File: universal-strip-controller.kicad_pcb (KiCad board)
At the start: 2 copper layers, 200 x 125 mm, 240 parts, among them J1 Conn_01x03_Pin, J10 DB301V-3.5-3P-GN, J11 DB301V-3.5-3P-GN, J12 DB301V-3.5-3P-GN, J13 DB301V-3.5-3P-GN, J14 DB301V-3.5-3P-GN, J15 DB301V-3.5-3P-GN, J16 DB301V-3.5-3P-GN, J17 DB301V-3.5-3P-GN, J18 DB301V-3.5-3P-GN, J19 DB301V-3.5-3P-GN, J2 Conn_01x02_Pin, J20 DB301V-3.5-3P-GN, J21 DB301V-3.5-3P-GN, J22 DB301V-3.5-3P-GN, J23 DB301V-3.5-3P-GN, J24 DB301V-3.5-3P-GN, J25 DB301V-3.5-3P-GN, J26 DB301V-3.5-3P-GN, J27 DB301V-3.5-3P-GN, J28 DB301V-3.5-3P-GN, J29 DB301V-3.5-3P-GN, J3 DBT50G-9.5-2P, J30 DB301V-3.5-3P-GN, J31 DB301V-3.5-3P-GN, J32 DB301V-3.5-3P-GN, J33 DB301V-3.5-3P-GN, J34 DB301V-3.5-3P-GN, J35 DB301V-3.5-3P-GN, J36 DB301V-3.5-3P-GN, J37 DB301V-3.5-3P-GN, J38 2.54-1*4, J39 DB301V-3.5-3P-GN, J4 DBT50G-9.5-2P, J5 DBT50G-9.5-2P, J6 DBT50G-9.5-2P, J7 DB301V-3.5-3P-GN, J8 DB301V-3.5-3P-GN, J9 DB301V-3.5-3P-GN, SW1 434133025816, SW2 434133025816, U1 RP2350B, U10 SN74LVC8T245PWR, U11 SN74LVC8T245PWR, U2 RPI RM2, U3 W25Q128JVSIQ, U4 SN74LVC1T45DBV, U5 TPS63070RNMR, U7 SN74LVC8T245PWR, U8 SN74LVC8T245PWR, U9 DS3231SN, X1 12MHz

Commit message: Working on layout
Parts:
- added C133: 100n, RPI_COMPILED:generic_capc1005x50, F.Cu at (209.5, 80.5)
- added C134: 100n, RPI_COMPILED:generic_capc1005x50, F.Cu at (209.5, 97.3)
- moved D12 371.3 mm to (214.3, 70.0), turned to 180 degrees
- moved C122 370.0 mm to (209.5, 72.0), turned to -90 degrees
- moved D16 362.8 mm to (214.3, 78.8), turned to 180 degrees
- moved C129 360.6 mm to (209.5, 88.5), turned to -90 degrees
- moved J23 360.1 mm to (226.5, 146.5), turned to 180 degrees
- moved D11 360.1 mm to (204.0, 70.0), turned to 180 degrees
- moved C121 359.4 mm to (199.0, 72.0), turned to -90 degrees
- moved C125 354.7 mm to (199.0, 80.5), turned to -90 degrees
- moved D20 354.6 mm to (214.3, 87.0), turned to 180 degrees
- moved C128 354.0 mm to (199.0, 88.5), turned to -90 degrees
- moved D15 351.7 mm to (204.0, 78.5), turned to 180 degrees
- moved C132 349.5 mm to (199.0, 97.5), turned to -90 degrees
- moved C120 349.4 mm to (189.0, 72.0), turned to -90 degrees
- moved D9 348.9 mm to (193.7, 70.0), turned to 180 degrees
- moved D24 346.5 mm to (214.3, 95.5), turned to 180 degrees
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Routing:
- net Net-(D11-DIN): track 0.00 -> 7.56 mm
- net Net-(D3-DOUT): track 0.00 -> 7.56 mm
- net Net-(D3-DIN): track 0.00 -> 5.36 mm
- net Net-(U4-B): track 0.00 -> 2.54 mm
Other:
- copper layers 2 -> 4

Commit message: Working on layout
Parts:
- moved F24 153.9 mm to (82.6, 150.8)
- moved J23 153.0 mm to (73.5, 148.6)
- moved J31 149.4 mm to (64.6, 133.2)
- moved F31 143.6 mm to (236.1, 150.8)
- moved J30 143.6 mm to (226.1, 148.6)
- moved F32 143.0 mm to (73.5, 137.9)
- moved J39 137.5 mm to (209.5, 133.2)
- moved F39 135.2 mm to (218.2, 139.2)
- moved F25 112.8 mm to (103.2, 150.8)
- moved J24 112.8 mm to (93.8, 148.6)
- moved F33 112.2 mm to (92.3, 137.9)
- moved J32 112.2 mm to (83.3, 133.2)
- moved J29 98.3 mm to (200.8, 148.6)
- moved F30 98.3 mm to (211.3, 150.8)
- moved F38 95.1 mm to (199.1, 137.9)
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
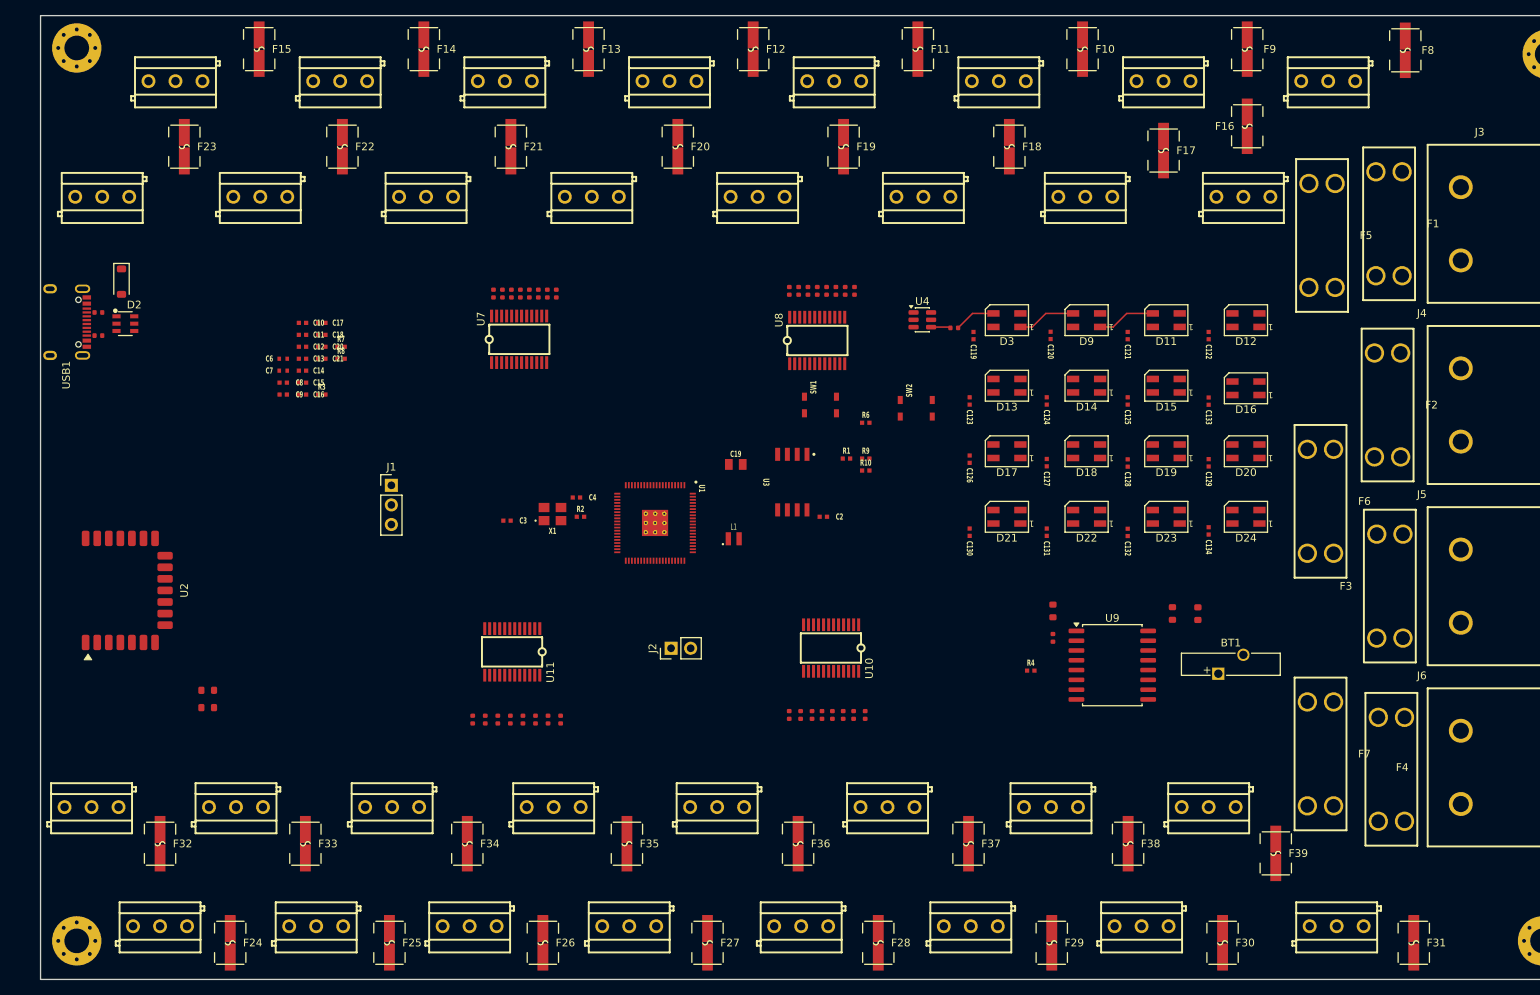
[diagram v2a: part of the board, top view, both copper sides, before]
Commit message: I think the output terminals are well-arranged now. Discovered pixel-blits layout all on my own.
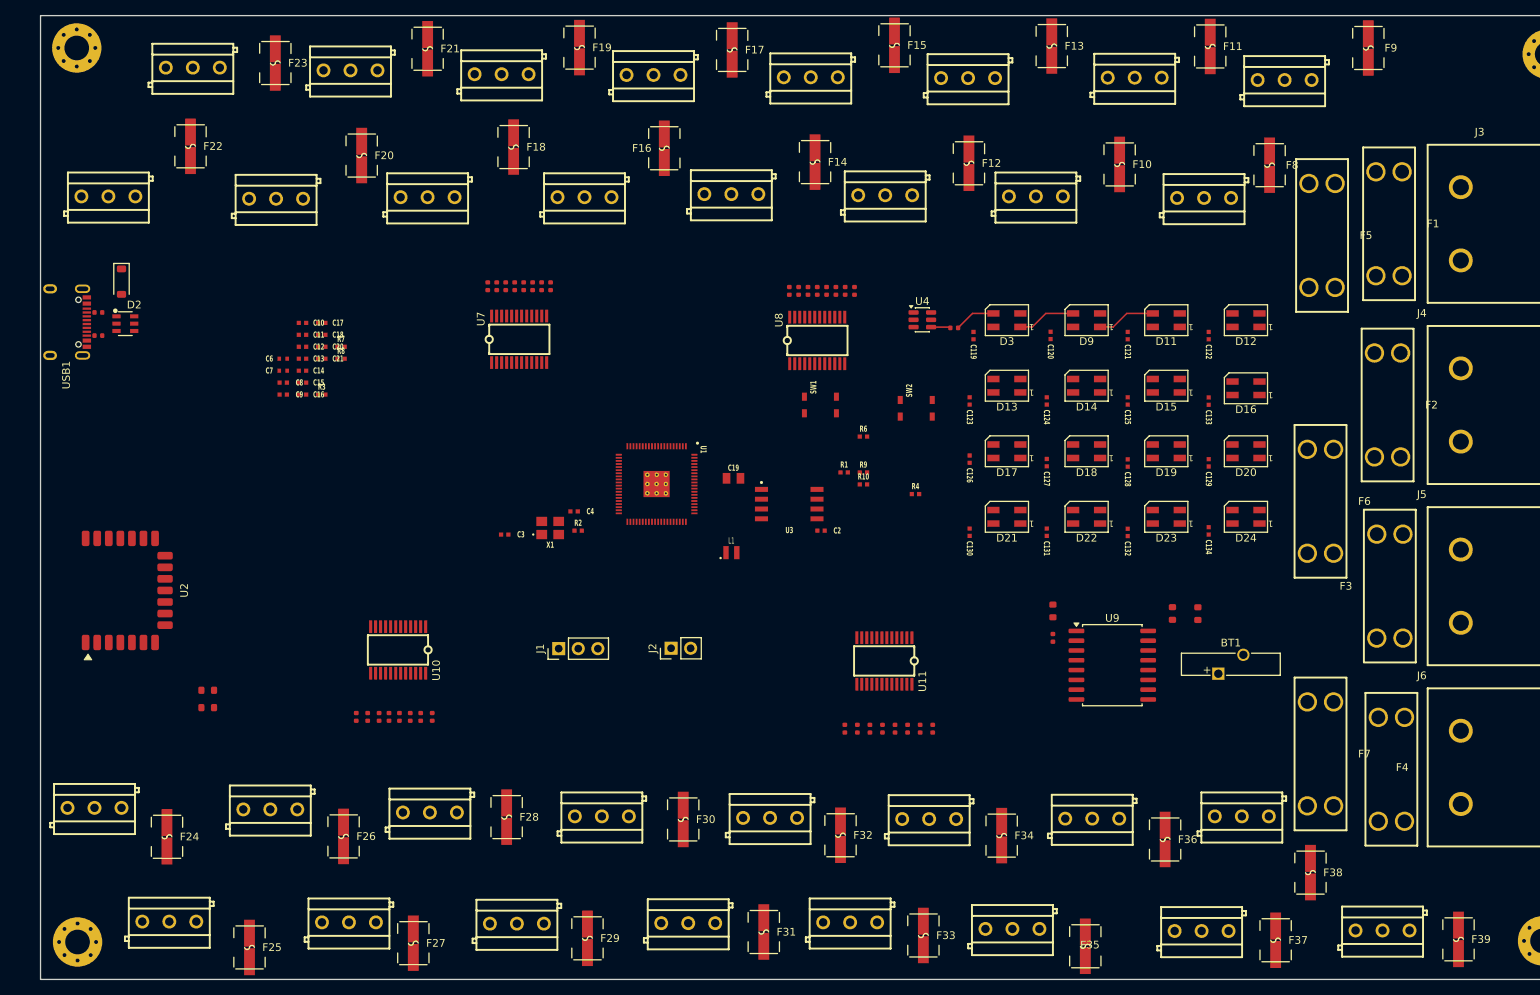
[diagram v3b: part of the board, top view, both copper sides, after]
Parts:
- moved F32 88.3 mm to (161.8, 136.8)
- moved J31 88.0 mm to (152.6, 134.6)
- moved J15 85.5 mm to (128.6, 54.0)
- moved F31 84.3 mm to (151.8, 149.3)
- moved J30 84.1 mm to (142.0, 148.2)
- moved F15 82.4 mm to (168.8, 34.4)
- moved J14 82.4 mm to (157.9, 38.5)
- moved J32 81.0 mm to (163.0, 148.1)
- moved F33 81.0 mm to (172.5, 149.8)
- moved F16 75.7 mm to (138.9, 47.7)
- moved F30 71.8 mm to (141.3, 134.8)
- moved J29 71.4 mm to (130.8, 134.3)
- moved J33 69.7 mm to (173.2, 134.7)
- moved F34 69.3 mm to (182.7, 136.8)
- moved F18 64.3 mm to (119.3, 47.5)
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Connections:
- F10 pad 1: +VIN_Z1 -> +VIN_Z2
- F12 pad 1: +VIN_Z1 -> +VIN_Z2
- F14 pad 1: +VIN_Z1 -> +VIN_Z2
- F17 pad 1: +VIN_Z2 -> +VIN_Z1
- F19 pad 1: +VIN_Z2 -> +VIN_Z1
- F21 pad 1: +VIN_Z2 -> +VIN_Z1
- F23 pad 1: +VIN_Z2 -> +VIN_Z1
- F25 pad 1: +VIN_Z3 -> +VIN_Z4
- F27 pad 1: +VIN_Z3 -> +VIN_Z4
- F29 pad 1: +VIN_Z3 -> +VIN_Z4
- F31 pad 1: +VIN_Z3 -> +VIN_Z4
- F32 pad 1: +VIN_Z4 -> +VIN_Z3
- F34 pad 1: +VIN_Z4 -> +VIN_Z3
- F36 pad 1: +VIN_Z4 -> +VIN_Z3
- F38 pad 1: +VIN_Z4 -> +VIN_Z3
- F8 pad 1: +VIN_Z1 -> +VIN_Z2

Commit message: Lined up the output connectors. Might actually be able to route this one
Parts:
- moved F39 8.96 mm to (233.0, 151.1)
- moved J39 8.96 mm to (223.1, 149.9)
- moved F37 5.74 mm to (212.5, 151.1)
- moved J36 5.73 mm to (202.9, 149.8)
- moved F38 3.30 mm to (219.4, 141.5)
- moved F28 2.94 mm to (116.5, 136.7)
- moved F30 2.72 mm to (139.4, 136.7)
- moved J25 2.67 mm to (85.5, 134.8)
- moved J27 2.49 mm to (106.2, 134.8)
- moved J29 2.34 mm to (128.5, 134.8)
- moved J37 2.34 mm to (211.5, 134.8)
- moved J31 2.31 mm to (150.3, 134.8)
- moved J35 2.30 mm to (192.1, 134.8)
- moved J33 2.30 mm to (170.9, 134.8)
- moved F36 2.01 mm to (201.9, 136.7)
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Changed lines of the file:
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@@
 	(footprint "EasyEDA:F1812"
 		(layer "F.Cu")
-		(at 172.5 149.8 -90)
+		(at 171.45 150.05 -90)
 		(property "Reference" "F33"
 			(at 0 -2.92 0)
@@
 	(footprint "PixelBlit:CONN-TH_DB301V-3.5-3P-GN"
 		(layer "F.Cu")
-		(at 88.55 54.25 180)
+		(at 88.55 54.15 180)
 		(property "Reference" "J19"
 			(at 0 -4 0)
@@
 	(footprint "PixelBlit:CONN-TH_DB301V-3.5-3P-GN"
 		(layer "F.Cu")
-		(at 194.4 134.65 180)
+		(at 192.1 134.8 180)
 		(property "Reference" "J35"
 			(at 0 -4 0)
@@
 	(footprint "EasyEDA:F1812"
 		(layer "F.Cu")
-		(at 178.407142 49.65 -90)
+		(at 177.907142 49.3 -90)
 		(property "Reference" "F12"
 			(at 0 -2.92 0)
@@
 	(footprint "EasyEDA:F1812"
 		(layer "F.Cu")
-		(at 147.7 34.95 -90)
+		(at 147.7 34.7 -90)
 		(property "Reference" "F17"
 			(at 0 -2.92 0)
@@
 	(footprint "PixelBlit:CONN-TH_DB301V-3.5-3P-GN"
 		(layer "F.Cu")
-		(at 167.55 53.8 180)
+		(at 167.55 54.15 180)
 		(property "Reference" "J11"
 			(at 0 -4 0)
@@
 	(footprint "EasyEDA:F1812"
 		(layer "F.Cu")
-		(at 203.85 137.35 -90)
+		(at 201.95 136.7 -90)
 		(property "Reference" "F36"
 			(at 0 -2.92 0)
@@
 	(footprint "PixelBlit:CONN-TH_DB301V-3.5-3P-GN"
 		(layer "F.Cu")
-		(at 147.592858 53.65 180)
+		(at 147.592858 54.15 180)
 		(property "Reference" "J13"
 			(at 0 -4 0)
@@
 	(footprint "EasyEDA:F1812"
 		(layer "F.Cu")
-		(at 127.9 34.65 -90)
+		(at 127.9 34.7 -90)
 		(property "Reference" "F19"
 			(at 0 -2.92 0)
@@
 	(footprint "PixelBlit:CONN-TH_DB301V-3.5-3P-GN"
 		(layer "F.Cu")
-		(at 119.7825 148.2675 180)
+		(at 118.7325 149.4 180)
 		(property "Reference" "J28"
 			(at 0 -4 0)
@@
 	(footprint "EasyEDA:F1812"
 		(layer "F.Cu")
-		(at 189.15 34.45 -90)
+		(at 189.15 34.7 -90)
 		(property "Reference" "F13"
 			(at 0 -2.92 0)
@@
 	(footprint "PixelBlit:CONN-TH_DB301V-3.5-3P-GN"
 		(layer "F.Cu")
-		(at 108.5 133.85 180)
+		(at 106.2 134.8 180)
 		(property "Reference" "J27"
 			(at 0 -4 0)
@@
 	(footprint "PixelBlit:CONN-TH_DB301V-3.5-3P-GN"
 		(layer "F.Cu")
-		(at 173.25 134.7 180)
+		(at 170.95 134.8 180)
 		(property "Reference" "J33"
 			(at 0 -4 0)
@@
 	(footprint "PixelBlit:CONN-TH_DB301V-3.5-3P-GN"
 		(layer "F.Cu")
-		(at 199.907143 38.55 180)
+		(at 199.907143 38.85 180)
 		(property "Reference" "J10"
 			(at 0 -4 0)
@@
 	(footprint "PixelBlit:CONN-TH_DB301V-3.5-3P-GN"
 		(layer "F.Cu")
-		(at 187.092857 53.95 180)
+		(at 187.092857 54.15 180)
 		(property "Reference" "J9"
 			(at 0 -4 0)
@@
 	(footprint "EasyEDA:F1812"
 		(layer "F.Cu")
-		(at 97.3 136.95 -90)
+		(at 95.4 136.7 -90)
 		(property "Reference" "F26"
 			(at 0 -2.92 0)
@@
 	(footprint "PixelBlit:CONN-TH_DB301V-3.5-3P-GN"
 		(layer "F.Cu")
-		(at 77.75 37.25 180)
+		(at 77.75 38.85 180)
 		(property "Reference" "J22"
 			(at 0 -4 0)
@@
 	(footprint "EasyEDA:F1812"
 		(layer "F.Cu")
-		(at 168.75 34.35 -90)
+		(at 168.75 34.7 -90)
 		(property "Reference" "F15"
 			(at 0 -2.92 0)
@@
 	(footprint "EasyEDA:F1812"
 		(layer "F.Cu")
-		(at 182.65 136.85 -90)
+		(at 180.75 136.7 -90)
 		(property "Reference" "F34"
 			(at 0 -2.92 0)
@@
 	(footprint "EasyEDA:F1812"
 		(layer "F.Cu")
-		(at 77.45 47.45 -90)
+		(at 76.95 49.3 -90)
 		(property "Reference" "F22"
 			(at 0 -2.92 0)
@@
 	(footprint "EasyEDA:F1812"
 		(layer "F.Cu")
-		(at 193.5 151.2 -90)
+		(at 192.45 151.45 -90)
 		(property "Reference" "F35"
 			(at -0.1825 -0.6025 0)
@@
 	(footprint "PixelBlit:CONN-TH_DB301V-3.5-3P-GN"
 		(layer "F.Cu")
-		(at 178.292858 38.6 180)
+		(at 178.292858 38.85 180)
 		(property "Reference" "J12"
 			(at 0 -4 0)
@@
 	(footprint "PixelBlit:CONN-TH_DB301V-3.5-3P-GN"
 		(layer "F.Cu")
-		(at 74.7 148 180)
+		(at 74.7 149.15 180)
 		(property "Reference" "J24"
 			(at 0 -4 0)
@@
 	(footprint "EasyEDA:F1812"
 		(layer "F.Cu")
-		(at 99.65 48.65 -90)
+		(at 99.15 49.3 -90)
 		(property "Reference" "F20"
 			(at 0 -2.92 0)
@@
 	(footprint "PixelBlit:CONN-TH_DB301V-3.5-3P-GN"
 		(layer "F.Cu")
-		(at 130.8 134.35 180)
+		(at 128.5 134.8 180)
 		(property "Reference" "J29"
 			(at 0 -4 0)
@@
 	(footprint "PixelBlit:CONN-TH_DB301V-3.5-3P-GN"
 		(layer "F.Cu")
-		(at 137.5 38.2 180)
+		(at 137.5 38.85 180)
 		(property "Reference" "J16"
 			(at 0 -4 0)
@@
 	(footprint "PixelBlit:CONN-TH_DB301V-3.5-3P-GN"
 		(layer "F.Cu")
-		(at 98.2 37.6 180)
+		(at 98.2 38.85 180)
 		(property "Reference" "J20"
 			(at 0 -4 0)
@@
 	(footprint "PixelBlit:CONN-TH_DB301V-3.5-3P-GN"
 		(layer "F.Cu")
-		(at 142 148.2 180)
+		(at 140.95 149.4 180)
 		(property "Reference" "J30"
 			(at 0 -4 0)
@@
 	(footprint "EasyEDA:F1812"
 		(layer "F.Cu")
-		(at 241.9 150.3 -90)
+		(at 232.976751 151.064188 -90)
 		(property "Reference" "F39"
 			(at 0 -2.92 0)
@@
 	(footprint "PixelBlit:CONN-TH_DB301V-3.5-3P-GN"
 		(layer "F.Cu")
-		(at 108.2 54.05 180)
+		(at 108.2 54.15 180)
 		(property "Reference" "J17"
 			(at 0 -4 0)
@@
 	(footprint "PixelBlit:CONN-TH_DB301V-3.5-3P-GN"
 		(layer "F.Cu")
-		(at 184.05 148.95 180)
+		(at 183 149.4 180)
 		(property "Reference" "J34"
 			(at 0 -4 0)
@@
 	(footprint "PixelBlit:CONN-TH_DB301V-3.5-3P-GN"
 		(layer "F.Cu")
-		(at 98 148.1 180)
+		(at 96.95 149.4 180)
 		(property "Reference" "J26"
 			(at 0 -4 0)
@@
 	(footprint "EasyEDA:F1812"
 		(layer "F.Cu")
-		(at 217.4 49.9 -90)
+		(at 216.9 49.3 -90)
 		(property "Reference" "F8"
 			(at 0 -2.92 0)
@@
 	(footprint "EasyEDA:F1812"
 		(layer "F.Cu")
-		(at 108.2 34.8 -90)
+		(at 108.2 34.7 -90)
 		(property "Reference" "F21"
 			(at 0 -2.92 0)
@@
 	(footprint "EasyEDA:F1812"
 		(layer "F.Cu")
-		(at 74.4 137 -90)
+		(at 74.8 136.45 -90)
 		(property "Reference" "F24"
 			(at 0 -2.92 0)
@@
 	(footprint "PixelBlit:CONN-TH_DB301V-3.5-3P-GN"
 		(layer "F.Cu")
-		(at 117.8 38.1 180)
+		(at 117.8 38.85 180)
 		(property "Reference" "J18"
 			(at 0 -4 0)
@@
 	(footprint "EasyEDA:F1812"
 		(layer "F.Cu")
-		(at 128.9325 150.1675 -90)
+		(at 127.8825 150.4175 -90)
 		(property "Reference" "F29"
 			(at 0 -2.92 0)
@@
 	(footprint "PixelBlit:CONN-TH_DB301V-3.5-3P-GN"
 		(layer "F.Cu")
-		(at 213.8 134.35 180)
+		(at 211.5 134.8 180)
 		(property "Reference" "J37"
 			(at 0 -4 0)
@@
 	(footprint "EasyEDA:F1812"
 		(layer "F.Cu")
-		(at 88.45 36.65 -90)
+		(at 88.15 34.7 -90)
 		(property "Reference" "F23"
 			(at 0 -2.92 0)
@@
 	(footprint "EasyEDA:F1812"
 		(layer "F.Cu")
-		(at 119.35 47.55 -90)
+		(at 118.85 49.3 -90)
 		(property "Reference" "F18"
 			(at 0 -2.92 0)
@@
 	(footprint "EasyEDA:F1812"
 		(layer "F.Cu")
-		(at 222.7 141.65 -90)
+		(at 219.4 141.5 -90)
 		(property "Reference" "F38"
 			(at 0 -2.92 0)
@@
 	(footprint "PixelBlit:CONN-TH_DB301V-3.5-3P-GN"
 		(layer "F.Cu")
-		(at 157.892858 38.5 180)
+		(at 157.892858 38.85 180)
 		(property "Reference" "J14"
 			(at 0 -4 0)
@@
 	(footprint "EasyEDA:F1812"
 		(layer "F.Cu")
-		(at 141.35 134.75 -90)
+		(at 139.45 136.7 -90)
 		(property "Reference" "F30"
 			(at 0 -2.92 0)
@@
 	(footprint "EasyEDA:F1812"
 		(layer "F.Cu")
-		(at 197.95 49.8 -90)
+		(at 197.45 49.3 -90)
 		(property "Reference" "F10"
 			(at 0 -2.92 0)
@@
 	(footprint "PixelBlit:CONN-TH_DB301V-3.5-3P-GN"
 		(layer "F.Cu")
-		(at 66.8 53.95 180)
+		(at 66.8 54.15 180)
 		(property "Reference" "J21"
 			(at 0 -4 0)
@@
 	(footprint "EasyEDA:F1812"
 		(layer "F.Cu")
-		(at 151.8 149.35 -90)
+		(at 150.75 149.6 -90)
 		(property "Reference" "F31"
 			(at 0 -2.92 0)
@@
 	(footprint "EasyEDA:F1812"
 		(layer "F.Cu")
-		(at 218.1825 150.4175 -90)
+		(at 212.4825 151.0675 -90)
 		(property "Reference" "F37"
 			(at 0 -2.92 0)
@@
 	(footprint "EasyEDA:F1812"
 		(layer "F.Cu")
-		(at 209.7 34.5 -90)
+		(at 209.7 34.7 -90)
 		(property "Reference" "F11"
 			(at 0 -2.92 0)
@@
 	(footprint "PixelBlit:CONN-TH_DB301V-3.5-3P-GN"
 		(layer "F.Cu")
-		(at 232.05 149.15 180)
+		(at 223.126751 149.914188 180)
 		(property "Reference" "J39"
 			(at 0 -4 0)
@@
 	(footprint "EasyEDA:F1812"
 		(layer "F.Cu")
-		(at 158.45 49.5 -90)
+		(at 157.95 49.3 -90)
 		(property "Reference" "F14"
 			(at 0 -2.92 0)
@@
 	(footprint "EasyEDA:F1812"
 		(layer "F.Cu")
-		(at 138.9 47.7 90)
+		(at 138.4 49.3 90)
 		(property "Reference" "F16"
 			(at 0 -2.92 0)
@@
 	(footprint "EasyEDA:F1812"
 		(layer "F.Cu")
-		(at 118.45 134.45 -90)
+		(at 116.55 136.7 -90)
 		(property "Reference" "F28"
 			(at 0 -2.92 0)
@@
 	(footprint "PixelBlit:CONN-TH_DB301V-3.5-3P-GN"
 		(layer "F.Cu")
-		(at 128.55 54.05 180)
+		(at 128.55 54.15 180)
 		(property "Reference" "J15"
 			(at 0 -4 0)
@@
 	(footprint "PixelBlit:CONN-TH_DB301V-3.5-3P-GN"
 		(layer "F.Cu")
-		(at 65 133.25 180)
+		(at 65 134.55 180)
 		(property "Reference" "J23"
 			(at 0 -4 0)
@@
 	(footprint "PixelBlit:CONN-TH_DB301V-3.5-3P-GN"
 		(layer "F.Cu")
-		(at 208.5825 149.2175 180)
+		(at 202.8825 149.8 180)
 		(property "Reference" "J36"
 			(at 0 -4 0)
@@
 	(footprint "PixelBlit:CONN-TH_DB301V-3.5-3P-GN"
 		(layer "F.Cu")
-		(at 87.8 133.45 180)
+		(at 85.5 134.8 180)
 		(property "Reference" "J25"
 			(at 0 -4 0)
@@
 	(footprint "EasyEDA:F1812"
 		(layer "F.Cu")
-		(at 161.75 136.8 -90)
+		(at 159.85 136.7 -90)
 		(property "Reference" "F32"
 			(at 0 -2.92 0)
@@
 	(footprint "EasyEDA:F1812"
 		(layer "F.Cu")
-		(at 106.35 150.8 -90)
+		(at 105.3 151.05 -90)
 		(property "Reference" "F27"
 			(at 0 -2.92 0)
@@
 	(footprint "PixelBlit:CONN-TH_DB301V-3.5-3P-GN"
 		(layer "F.Cu")
-		(at 152.6175 134.55 180)
+		(at 150.3175 134.8 180)
 		(property "Reference" "J31"
 			(at 0 -4 0)
@@
 	(footprint "PixelBlit:CONN-TH_DB301V-3.5-3P-GN"
 		(layer "F.Cu")
-		(at 163 148.1 180)
+		(at 161.95 149.4 180)
 		(property "Reference" "J32"
 			(at 0 -4 0)
